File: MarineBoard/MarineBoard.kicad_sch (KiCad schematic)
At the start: 157 parts, among them CN1 MKDSN 1,5/ 2-5,08, CN2 MKDSN 1,5/ 2-5,08, CN3 SM04B-SRSS-TB (LF)(SN), J1 USB_C_Receptacle_USB2.0_16P, Q2 S8050, Q3 S8050, Q4 BUK762R4-60E, U1 SY8089A1AAC, U10 SM10B-GHS-TB, U11 SN65HVD230DR, U12 DB125-3.5-3P-GN-S, U13 DB125-3.5-3P-GN-S, U14 PC817C-S, U16 PC817C-S, U17 PC817C-S, U18 INA226, U19 INA226, U2 INA226, U21 PC817C-S, U22 SN74LVC1G14DBVR, U23 MCP1407-E/MF_C640313, U3 TPS5430DDA, U4 DB125-3.5-2P-GN-S, U5 DB125-3.5-2P-GN-S, U6 DB125-3.5-2P-GN-S, U7 DB125-3.5-3P-GN-S, U8 ESP32-S3-WROOM-2-N32R16V, U9 DB125-3.5-3P-GN-S

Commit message: MarineBoard: R16 part = C25718 (10k 1W 200V 2512) (#26)
Co-Authored-By: Claude Opus 5.5 <noreply@anthropic.com>
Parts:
- R16: MPN 25121WF1002T4E -> C25718
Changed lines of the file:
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@@
 			)
 		)
-		(property "MPN" "25121WF1002T4E"
+		(property "MPN" "C25718"
 			(at 174.498 169.418 0)
 			(show_name no)

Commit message: MarineBoard: fill missing MPNs (J1, R6, C16, C17 + SUPPLIERPART copies for Q2/Q3, D2/D3, L3/L4/L6)
Co-Authored-By: Claude Opus 5.5 <noreply@anthropic.com>
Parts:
- C16: MPN (none) -> C51205
- C17: MPN (none) -> C13585
- D2, D3: MPN (none) -> C7420372
- J1: MPN (none) -> C2894897
- L3, L4, L6: MPN (none) -> C79382
- Q2, Q3: MPN (none) -> C20069125
- R6: MPN (none) -> C25105
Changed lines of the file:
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@@
 			)
 		)
+		(property "MPN" "C20069125"
+			(at 295.91 93.98 90)
+			(hide yes)
+			(show_name no)
+			(do_not_autoplace no)
+			(effects
+				(font
+					(size 1.27 1.27)
+				)
+				(justify right top)
+			)
+		)
 		(property "Description" "晶体管类型:NPN;集电极电流(Ic):500mA;集射极击穿电压(Vceo):25V;耗散功率(Pd):300mW;直流电流增益(hFE):120@50mA,1.0V;"
 			(at 295.91 93.98 0)
@@
 			)
 		)
+		(property "MPN" "C7420372"
+			(at 95.25 52.07 90)
+			(hide yes)
+			(show_name no)
+			(do_not_autoplace no)
+			(effects
+				(font
+					(size 1.27 1.27)
+				)
+				(justify right top)
+			)
+		)
 		(property "Description" "极性:双向;反向截止电压(Vrwm):5V;钳位电压:10V;峰值脉冲电流(Ipp):5A;峰值脉冲功率(Ppp):50W;击穿电压:5.6V;"
 			(at 95.25 52.07 0)
@@
 			)
 		)
-		(property "MPN" ""
+		(property "MPN" "C25105"
 			(at 100.33 43.18 90)
 			(hide yes)
@@
 			)
 		)
+		(property "MPN" "C20069125"
+			(at 330.2 274.32 90)
+			(hide yes)
+			(show_name no)
+			(do_not_autoplace no)
+			(effects
+				(font
+					(size 1.27 1.27)
+				)
+				(justify right top)
+			)
+		)
 		(property "Description" "晶体管类型:NPN;集电极电流(Ic):500mA;集射极击穿电压(Vceo):25V;耗散功率(Pd):300mW;直流电流增益(hFE):120@50mA,1.0V;"
 			(at 330.2 274.32 0)
@@
 			)
 		)
-		(property "MPN" ""
+		(property "MPN" "C51205"
 			(at 72.39 90.17 90)
 			(hide yes)
@@
 			)
 		)
-		(property "MPN" ""
+		(property "MPN" "C13585"
 			(at 82.55 106.68 0)
 			(hide yes)
@@
 			)
 		)
+		(property "MPN" "C79382"
+			(at 203.2 96.52 90)
+			(hide yes)
+			(show_name no)
+			(do_not_autoplace no)
+			(effects
+				(font
+					(size 1.27 1.27)
+				)
+				(justify right top)
+			)
+		)
 		(property "Description" "标称阻抗@测试频率:120Ω@100MHz;误差:±25%;直流电阻(RDC):30mΩ;"
 			(at 203.2 96.52 0)
@@
 			)
 		)
+		(property "MPN" "C2894897"
+			(at 71.12 39.37 0)
+			(hide yes)
+			(show_name no)
+			(do_not_autoplace no)
+			(effects
+				(font
+					(size 1.27 1.27)
+				)
+			)
+		)
 		(property "Description" "USB 2.0-only 16P Type-C Receptacle connector"
 			(at 67.31 39.37 0)
@@
 			)
 		)
+		(property "MPN" "C79382"
+			(at 110.49 77.47 90)
+			(hide yes)
+			(show_name no)
+			(do_not_autoplace no)
+			(effects
+				(font
+					(size 1.27 1.27)
+				)
+				(justify right top)
+			)
+		)
 		(property "Description" "标称阻抗@测试频率:120Ω@100MHz;误差:±25%;直流电阻(RDC):30mΩ;"
 			(at 110.49 77.47 0)
@@
 			)
 		)
+		(property "MPN" "C79382"
+			(at 69.85 77.47 90)
+			(hide yes)
+			(show_name no)
+			(do_not_autoplace no)
+			(effects
+				(font
+					(size 1.27 1.27)
+				)
+				(justify right top)
+			)
+		)
 		(property "Description" "标称阻抗@测试频率:120Ω@100MHz;误差:±25%;直流电阻(RDC):30mΩ;"
 			(at 69.85 77.47 0)
@@
 			(at 95.25 33.02 90)
 			(hide yes)
+			(show_name no)
+			(do_not_autoplace no)
+			(effects
+				(font
+					(size 1.27 1.27)
+				)
+				(justify right top)
+			)
+		)
+		(property "MPN" "C7420372"
+			(at 95.25 33.02 90)
+			(hide yes)

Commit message: MarineBoard v1.9: RGB status LED, vertical CN4 display header, logo, fab package (#179)
- D17 plain LED -> D5 WS2812B-2020-V6 (C52917434) on GPIO1, VDD +5V_VCC,
  C40 decoupling, R34 100R on DIN
- U10 right-angle GH on the bottom -> CN4 vertical BM10B-GHS-TBT on top
  (pinout unchanged); all fuses/connectors on top; GND stitching reworked
- Sisu logo + "MARINE BOARD v1.9" silk (LOGO1), RESET/FLASH labels
- Libraries consolidated back into Lib/ (root EasyEDA.* retired), CN4
  courtyard now covers its leads, L2 footprint attr THT -> SMD
- fab_package.py rebuilds production/ (DRC gate, gerbers/drill/IPC zip,
  BOM + centroid CSV/XLSX with LOOSE rows); stale production files removed
- Technical Specs v1.9 (CN4, RGB LED, fab script, U5/U6/U7 pin order),
  system spec 2.15, README, feature map, HEADER PINS / LEDS exports

Firmware follow-up for the RGB LED: #180

Co-Authored-By: Claude Opus 5.5 <noreply@anthropic.com>
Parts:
- removed D17: LED, LED_SMD:LED_0603_1608Metric, symbol Device:LED
- removed R34: 470R, Resistor_SMD:R_0402_1005Metric, symbol Device:R
- removed U10: SM10B-GHS-TB, LCSC:CONN-SMD_SM10B-GHS-TB, symbol LCSC:SM10B-GHS-TB
- added C40: 0.1uF, Capacitor_SMD:C_0402_1005Metric, symbol Device:C
- added CN4: BM10B-GHS-TBT, LCSC:CONN-SMD_BM10B-GHS-TBT-LF-SN, symbol LCSC:BM10B-GHS-TBT
- added D5: WS2812B-2020, LED_SMD:LED_WS2812B-2020_PLCC4_2.0x2.0mm, symbol LED:WS2812B-2020
- added R34: 100, LCSC:R0402, symbol LCSC:0402WGF1000TCE
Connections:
- net +3.3V: now also CN4.1
- net +5V: now also C40.2, CN4.10, D5.4 (VDD)
- net BL/GPIO18: now also CN4.9
- net CS0/GPIO10: now also CN4.6
- net DC/GPIO9: now also CN4.7
- net GND: now also C40.1, CN4.11, CN4.12, CN4.2, D5.2 (VSS)
- net LED: now also R34.2
- net MISO/GPIO13: now also CN4.5
- net MOSI/GPIO11: now also CN4.4
- net RST/GPIO14: now also CN4.8
- net SCK/GPIO12: now also CN4.3
- new net: D5.3 (DIN), R34.1
- no-connect marks 19 -> 20
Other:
- moved on the sheet: BUZZER1, C34, C35, Flash1, R27, R28, Reset1

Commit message: MarineBoard v1.9.1 pre-fab fixes: U3 ENA float, 50V caps, polymer C20 (#183)
- U3 TPS5430 ENA (pin 5) disconnected from VIN_BUCK (7 V abs max) and left
  floating per TI; schematic wires + PCB stub removed, no-connect added.
- C11/C12/C14/C19/C42 -> CL05B104KB5NNNC (50 V; were 16 V on 12 V/bus nets),
  C33 -> 1 uF 50 V GRM155R61H105KE05D (was 4.7 uF 10 V on +12V BAT).
- C20 -> Panasonic 10SVPE220M 20 mOhm polymer: 15 uH + 220 uF <=40 mOhm is
  TI's internal-compensation reference; the copied ceramic-cap network
  C21/C22/R13/C23 (TI Fig 7-11, 3.3 V/100 uF design) is now DNP.
- Order sheet File Name -> MarineBoard-PCBWay-Gerbers.zip.
- Fab package rebuilt; DRC (schematic parity) and ERC unchanged vs before.

Still open in #183 (routing, human): U2 VBUS, U23 supply rail, C15, D5.

Co-Authored-By: Claude Opus 5.5 <noreply@anthropic.com>
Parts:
- C11, C12, C14, C19, C42: MPN CL05B104KO5NNNC -> CL05B104KB5NNNC
- C20: MPN C72494 -> 10SVPE220M; Manufacturer Lelon -> Panasonic
- C21, C22, C23, R13: now not fitted
- C33: value 4.7uF -> 1uF; MPN CL05A475MP5NRNC -> GRM155R61H105KE05D; Manufacturer Samsung Electro-Mechanics -> muRata
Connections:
- net VIN_BUCK: no longer U3.5 (EN)
- no-connect marks 20 -> 21
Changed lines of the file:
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@@
 	)
 	(junction
-		(at 88.9 91.44)
-		(diameter 0)
-		(color 0 0 0 0)
-	)
-	(junction
 		(at 387.35 236.22)
 		(diameter 0)
@@
 		(at 370.84 161.29)
 	)
+	(no_connect
+		(at 90.17 101.6)
+	)
 	(wire
 		(pts
@@
 	(wire
 		(pts
-			(xy 88.9 101.6) (xy 90.17 101.6)
-		)
-		(stroke
-			(width 0)
-			(type default)
-		)
-	)
-	(wire
-		(pts
 			(xy 259.08 24.13) (xy 257.81 24.13)
 		)
@@
 	(wire
 		(pts
-			(xy 88.9 91.44) (xy 88.9 101.6)
-		)
-		(stroke
-			(width 0)
-			(type default)
-		)
-	)
-	(wire
-		(pts
 			(xy 74.93 250.19) (xy 77.47 250.19)
 		)
@@
 			)
 		)
-		(property "Datasheet" ""
+		(property "Datasheet" "~"
 			(at 368.3 99.06 0)
 			(hide yes)
@@
 			)
 		)
-		(property "MPN" "CL05B104KO5NNNC"
+		(property "MPN" "CL05B104KB5NNNC"
 			(at 368.3 99.06 0)
 			(hide yes)
@@
 			)
 		)
-		(property "Datasheet" "https://www.lcsc.com/datasheet/C1525.pdf"
+		(property "Datasheet" "~"
 			(at 143.51 83.82 0)
 			(hide yes)
@@
 			)
 		)
-		(property "Description" "Unpolarized capacitor"
+		(property "Description" "100nF ±10% 50V Ceramic Capacitor X7R 0402"
 			(at 143.51 83.82 0)
 			(hide yes)
@@
 			)
 		)
-		(property "MPN" "CL05B104KO5NNNC"
+		(property "MPN" "CL05B104KB5NNNC"
 			(at 143.51 83.82 0)
 			(hide yes)
@@
 		(on_board yes)
 		(in_pos_files yes)
-		(dnp no)
+		(dnp yes)
 		(property "Reference" "C23"
 			(at 196.85 110.4899 90)
@@
 			)
 		)
-		(property "Value" "4.7uF"
+		(property "Value" "1uF"
 			(at 231.394 226.314 0)
 			(show_name no)
@@
 			)
 		)
-		(property "Datasheet" "https://lcsc.com/product-detail/Multilayer-Ceramic-Capacitors-MLCC-SMD-SMT_SAMSUNG_CL05A475MP5NRNC_4-7uF-475-20-10V_C23733.html"
+		(property "Datasheet" "~"
 			(at 232.41 219.71 0)
 			(hide yes)
@@
 			)
 		)
-		(property "Description" "4.7uF ±20% 10V Ceramic Capacitor X5R 0402"
+		(property "Description" "1uF ±10% 50V Ceramic Capacitor X5R 0402"
 			(at 232.41 232.41 0)
 			(hide yes)
@@
 			)
 		)
-		(property "MPN" "CL05A475MP5NRNC"
+		(property "MPN" "GRM155R61H105KE05D"
 			(at 232.41 232.41 90)
 			(hide yes)
@@
 			)
 		)
-		(property "Manufacturer" "Samsung Electro-Mechanics"
+		(property "Manufacturer" "muRata"
 			(at 232.41 232.41 90)
 			(hide yes)
@@
 		(on_board yes)
 		(in_pos_files yes)
-		(dnp no)
+		(dnp yes)
 		(property "Reference" "C21"
 			(at 197.104 99.06 90)
@@
 		(on_board yes)
 		(in_pos_files yes)
-		(dnp no)
+		(dnp yes)
 		(property "Reference" "R13"
 			(at 212.09 111.7599 90)
@@
 		(on_board yes)
 		(in_pos_files yes)
-		(dnp no)
+		(dnp yes)
 		(property "Reference" "C22"
 			(at 205.105 98.933 90)
@@
 			)
 		)
-		(property "Datasheet" "https://www.lcsc.com/datasheet/C1525.pdf"
+		(property "Datasheet" "~"
 			(at 360.68 66.04 0)
 			(hide yes)
@@
 			)
 		)
-		(property "Description" "Unpolarized capacitor"
+		(property "Description" "100nF ±10% 50V Ceramic Capacitor X7R 0402"
 			(at 360.68 66.04 0)
 			(hide yes)
@@
 			)
 		)
-		(property "MPN" "CL05B104KO5NNNC"
+		(property "MPN" "CL05B104KB5NNNC"
 			(at 360.68 66.04 0)
 			(hide yes)
@@
 			)
 		)
-		(property "Datasheet" "https://www.lcsc.com/datasheet/C1525.pdf"
+		(property "Datasheet" "~"
 			(at 54.61 96.52 0)
 			(hide yes)
@@
 			)
 		)
-		(property "Description" "Unpolarized capacitor"
+		(property "Description" "100nF ±10% 50V Ceramic Capacitor X7R 0402"
 			(at 54.61 96.52 0)
 			(hide yes)
@@
 			)
 		)
-		(property "MPN" "CL05B104KO5NNNC"
+		(property "MPN" "CL05B104KB5NNNC"
 			(at 54.61 96.52 0)
 			(hide yes)
@@
 			)
 		)
-		(property "Datasheet" "https://www.lcsc.com/datasheet/C1525.pdf"
+		(property "Datasheet" "~"
 			(at 358.14 60.96 0)
 			(hide yes)
@@
 			)
 		)
-		(property "Description" "Unpolarized capacitor"
+		(property "Description" "100nF ±10% 50V Ceramic Capacitor X7R 0402"
 			(at 358.14 60.96 0)
 			(hide yes)
@@
 			)
 		)
-		(property "MPN" "CL05B104KO5NNNC"
+		(property "MPN" "CL05B104KB5NNNC"
 			(at 358.14 60.96 0)
 			(hide yes)
@@
 			)
 		)
-		(property "Datasheet" ""
+		(property "Datasheet" "~"
 			(at 170.18 118.11 0)
 			(hide yes)
@@
 			)
 		)
-		(property "Description" "220uF ±20% 10V Aluminum Electrolytic Capacitor 6.3x5.4mm"
+		(property "Description" "220uF ±20% 10V OS-CON polymer, ESR 20mΩ, SMD D6.3xL5.9mm (TPS5430 internal comp needs ESR <=40mΩ)"
 			(at 170.18 130.81 0)
 			(hide yes)
@@
 			)
 		)
-		(property "Manufacturer" "Lelon"
+		(property "Manufacturer" "Panasonic"
 			(at 170.18 120.65 0)
 			(hide yes)
@@
 			)
 		)
-		(property "MPN" "C72494"
+		(property "MPN" "10SVPE220M"
 			(at 176.276 105.918 90)
 			(show_name no)

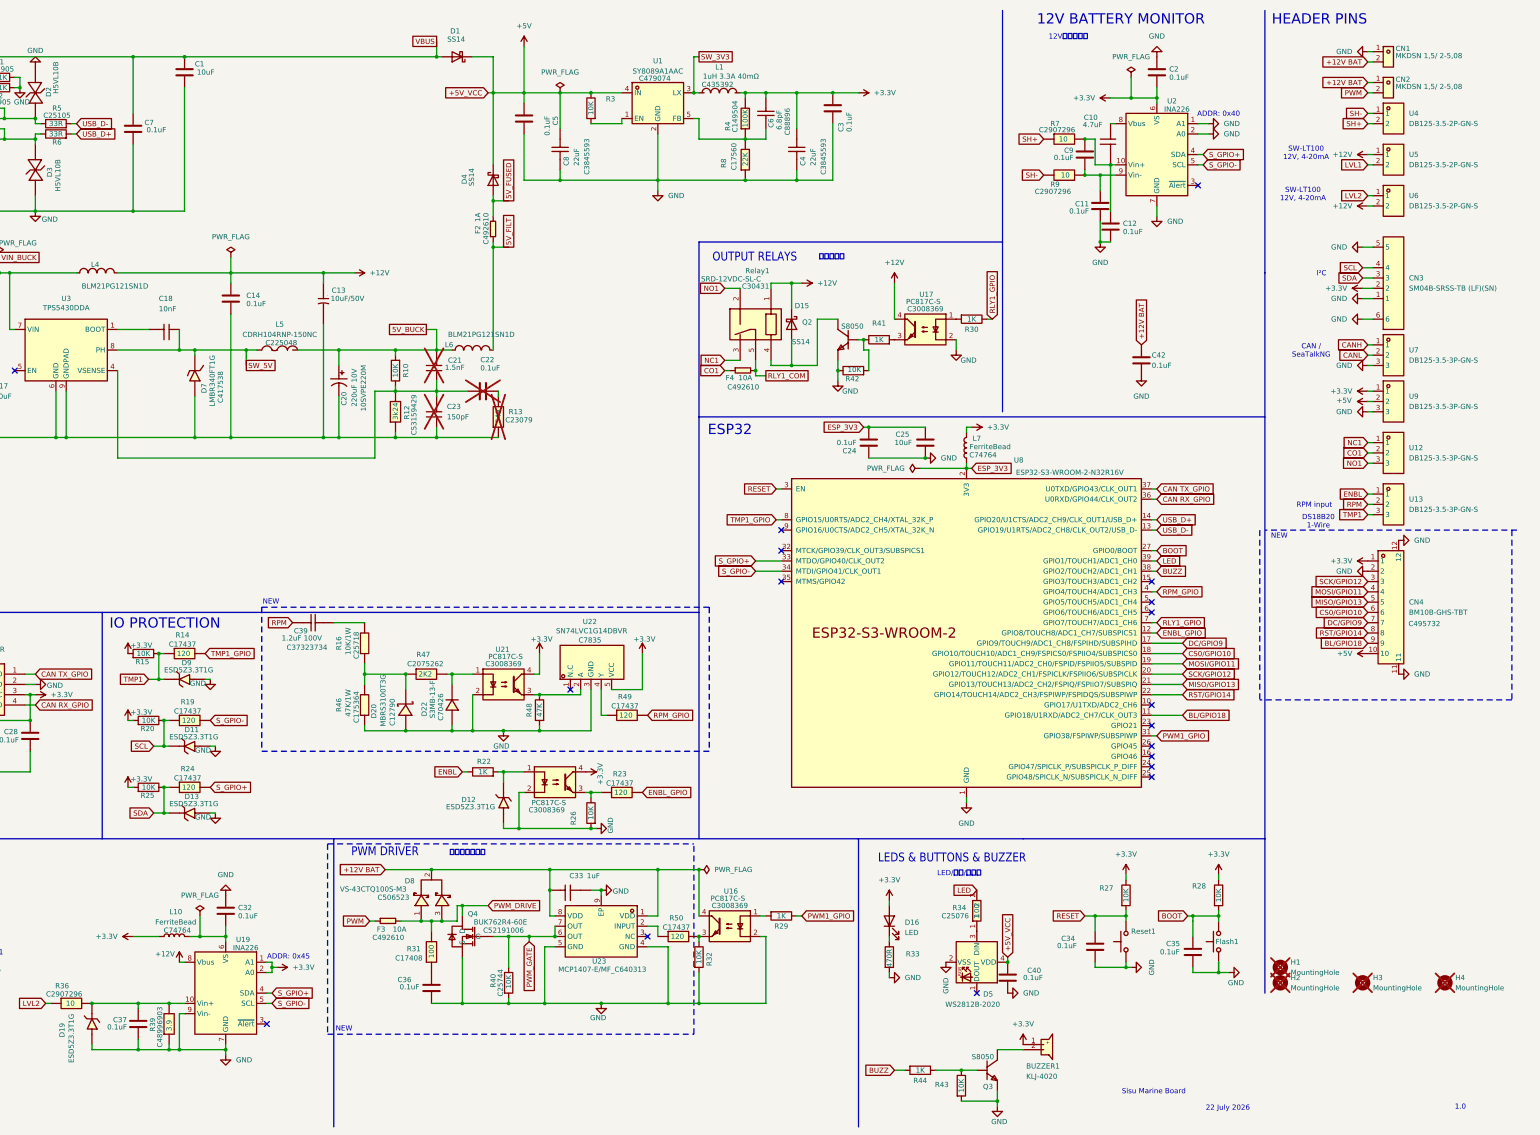
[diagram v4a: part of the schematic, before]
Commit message: MarineBoard 1.9.1 schematic: U23 on +12V, D5 via D21, test pads, CAN GPIO5/6 (#183)
Human edits (KiCad): buck add-on network removed, U2 VBUS tied to Vin+
(high-side shunt) with series C10 removed, D17 SS14 buzzer flyback,
CAN moved to GPIO5 TX / GPIO6 RX.

Agent edits:
- U23 MCP1407: pin 8 had been moved to +5V_VCC while pin 1 stayed on
  +12V BAT (both are VDD -> rail short; and 5 V gate drive is too low for
  standard-level Q4). Both VDD pins + C33 now on protected +12V.
- D5 WS2812B VDD fed through D21 1N4148W (~4.35 V) so 3.3 V data meets VIH;
  PWR_FLAG on the new VDD node.
- TP1-TP6 bare 1.5 mm pads (no BOM/pos): GND, +12V, +5V_VCC, +3.3V,
  PWM_GATE, VSENSE; U3 feedback node labelled VSENSE.
- bench_marine_board.yaml CAN RX probe -> GPIO6 (deployed to HA Green).
- Technical Specs: GPIO/CAN tables, buck note, 1.9.1 revision row.
- C15 kept at 25 V (accepted; a 50 V 1206 loses input-filter damping).

ERC unchanged vs baseline (2 pre-existing D5 flags). PCB not yet updated
from schematic: routing pending, fab package not rebuilt.

Co-Authored-By: Claude Opus 5.5 <noreply@anthropic.com>
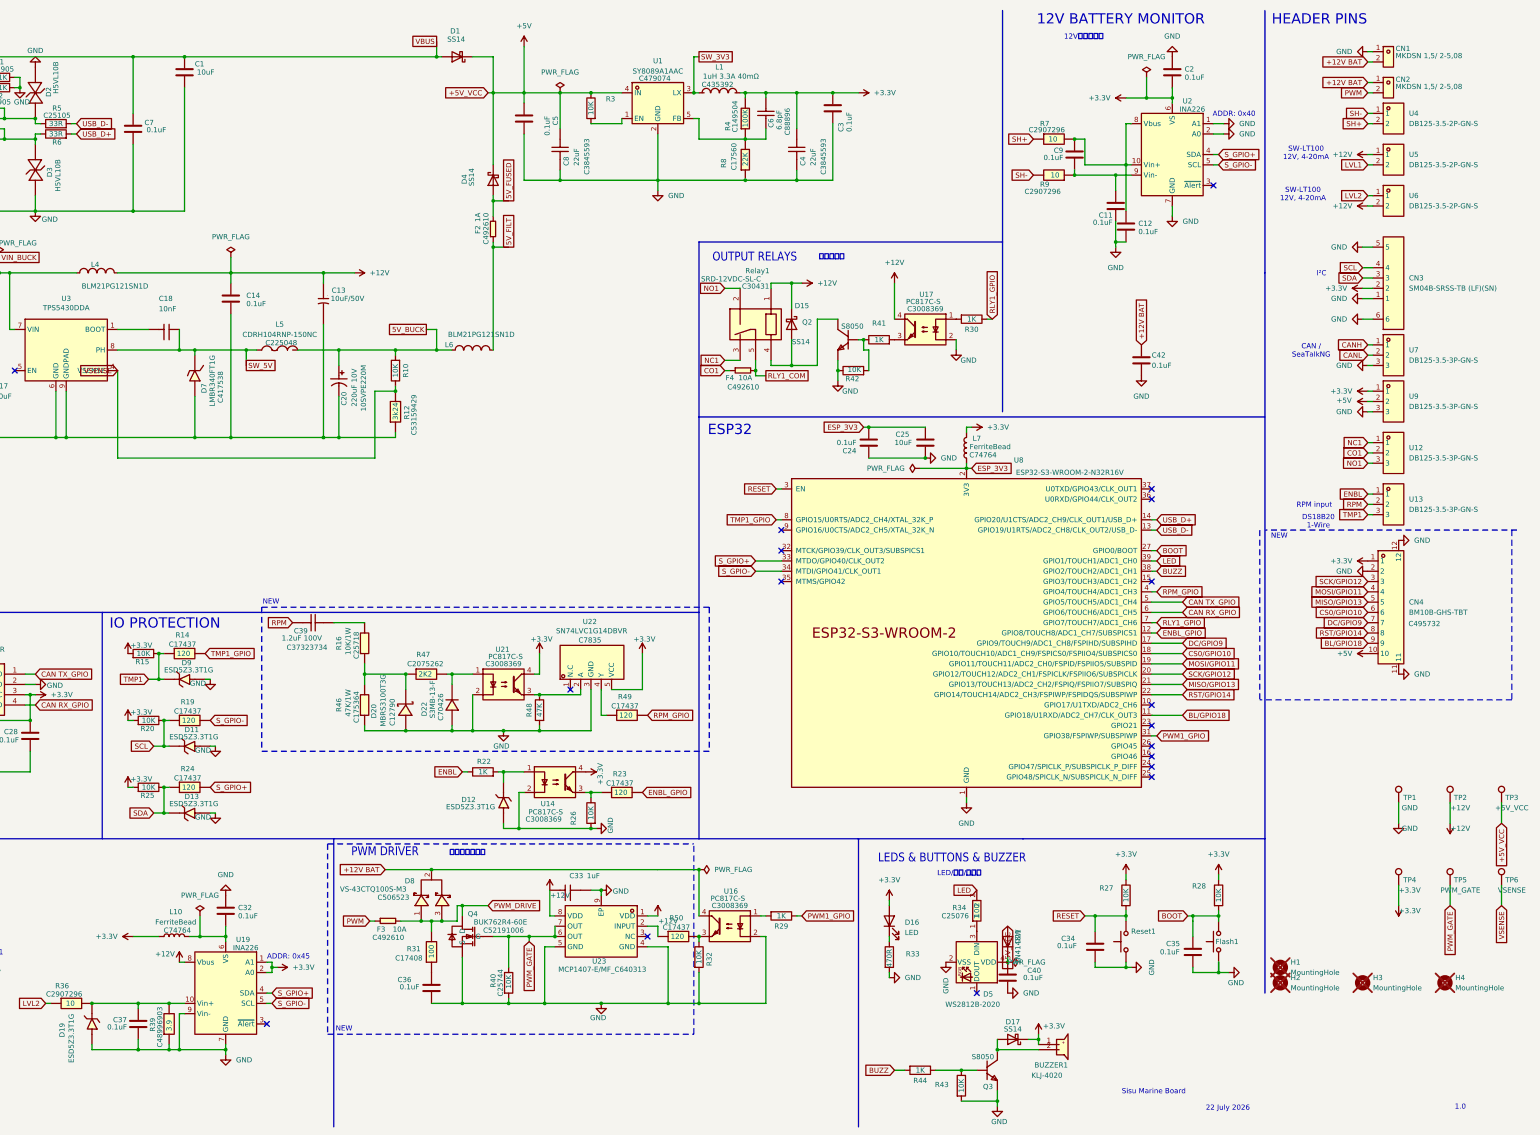
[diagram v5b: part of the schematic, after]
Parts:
- removed C10: 4.7uF, Capacitor_SMD:C_0402_1005Metric, symbol CL05A475MP5NRNC
- removed C21: 1.5nF, Capacitor_SMD:C_0402_1005Metric, symbol 0603B152K500NT
- removed C22: 0.1uF, Capacitor_SMD:C_0402_1005Metric, symbol Device:C
- removed C23: 150pF, Capacitor_SMD:C_0402_1005Metric, symbol 0603B151K500NT
- removed R13: 549, Resistor_SMD:R_0603_1608Metric, symbol 0603WAF5490T5E
- added D17: SS14, Diode_SMD:D_SMA, symbol Diode:SS14
- added D21: 1N4148W, Diode_SMD:D_SOD-123, symbol Device:D
- added TP1: GND, TestPoint:TestPoint_Pad_D1.5mm, symbol Connector:TestPoint
- added TP2: +12V, TestPoint:TestPoint_Pad_D1.5mm, symbol Connector:TestPoint
- added TP3: +5V_VCC, TestPoint:TestPoint_Pad_D1.5mm, symbol Connector:TestPoint
- added TP4: +3.3V, TestPoint:TestPoint_Pad_D1.5mm, symbol Connector:TestPoint
- added TP5: PWM_GATE, TestPoint:TestPoint_Pad_D1.5mm, symbol Connector:TestPoint
- added TP6: VSENSE, TestPoint:TestPoint_Pad_D1.5mm, symbol Connector:TestPoint
- C14: JLCPCB ID (none) -> C960916
- C33: JLCPCB ID (none) -> C1518208
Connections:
- net +12V: now also C33.2, U23.1 (VDD), U23.8 (VDD), TP2.1
- net +12V BAT: no longer C33.2, U23.1 (VDD), U23.8 (VDD)
- net +3.3V: now also D17.1 (K), TP4.1
- net +5V: now also D21.2 (A), TP3.1; no longer C40.2, D5.4 (VDD)
- net CAN RX_GPIO: now also U8.6 (GPIO6/TOUCH6/ADC1_CH5); no longer U8.36 (U0RXD/GPIO44/CLK_OUT2)
- net CAN TX_GPIO: now also U8.5 (GPIO5/TOUCH5/ADC1_CH4); no longer U8.37 (U0TXD/GPIO43/CLK_OUT1)
- net GND: now also TP1.1
- net PWM_GATE: now also TP5.1
- net at C12.1, C9.2, R7.2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: now also U2.8 (Vbus)
- net at BUZZER1.2 (-), Q3.3 (C): now also D17.2 (A)
- net VSENSE: now reaches R10.1, R12.2, U3.4 (VSENSE)
- net VSENSE: now also TP6.1
- new net: C40.2, D21.1 (K), D5.4 (VDD)
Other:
- moved on the sheet: BUZZER1, C11, C12, C2, C9, R7, R9, U2
